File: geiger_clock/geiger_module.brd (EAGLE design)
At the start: 25 x 128.5 mm, 39 parts, among them IC2 7805TV, IC3 74125N, Q1 FJN3303F, Q2 2N3904, Q3 2N3904, U1 TLC555CP, U2 ATTINY2313, X1 8MHz

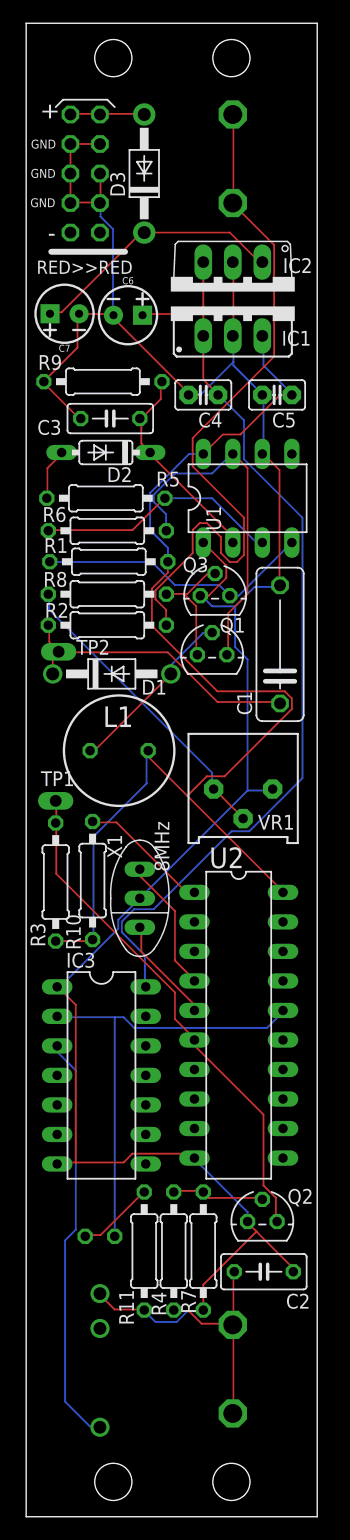
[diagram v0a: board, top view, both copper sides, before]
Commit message: updated the geiger module
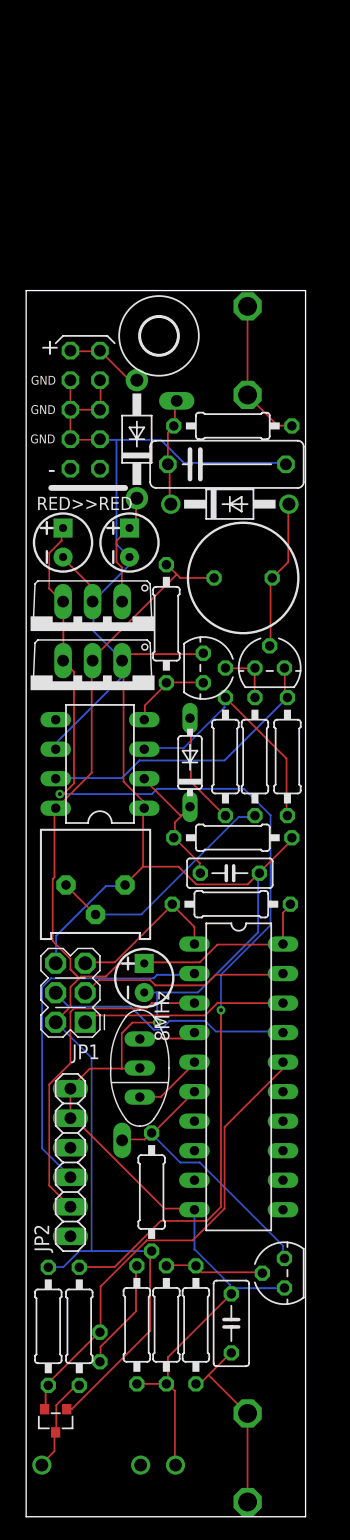
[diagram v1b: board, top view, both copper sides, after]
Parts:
- removed C5: 10uF, capacitor-wima:C2.5-2
- removed IC1: (no value), v-reg-3:78XXS
- added H1: MOUNT-HOLE3.2, holes:3,2
- added JP1: (no value), arduino_jw:CONN-2X03
- added JP2: (no value), pinhead:1X06
- added Q4: BSS138, bss138_10:SOT23
- added R12, R13: 10k, resistor:0207/10
- C4: device capacitor-wima:C2.5-2 -> SparkFun-Capacitors:CPOL-RADIAL-2.5MM-5MM
- IC3: value 74125N -> LM1117T(V)-3.3; device 74xx-us:DIL14 -> lm1117_10:TO220V
- moved C4 50.4 mm to (10.2, 46.4), turned to 90 degrees
- moved R9 40.8 mm to (17.8, 58.4), turned to 180 degrees
- moved C3 40.4 mm to (17.5, 55.4), turned to 0 degrees
- moved IC3 33.2 mm to (5.71, 71.1), turned to 180 degrees
- moved IC2 31.6 mm to (5.71, 76.2)
- moved TP1 29.8 mm to (8.26, 32.4), turned to 270 degrees
- moved R3 27.9 mm to (10.8, 27.9)
- moved D2 27.6 mm to (14.1, 64.9), turned to 90 degrees
- moved U1 26.2 mm to (6.35, 64.8), turned to 90 degrees
- moved R6 24.9 mm to (22.5, 65.4), turned to 90 degrees
- moved R5 24.5 mm to (17.1, 65.4), turned to 90 degrees
- moved TP2 23.9 mm to (13.0, 96.0)
- moved D3 22.9 mm to (9.53, 92.7)
- moved C7 20.5 mm to (8.89, 83.8), turned to 90 degrees
- moved C6 20.3 mm to (3.17, 83.8), turned to 90 degrees
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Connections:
- new net N$13: JP1.1, U2.18
- new net N$16: JP1.4, U2.17
- new net N$5: JP1.3, U2.19
- new net N$6: JP2.2, U2.3
- new net N$7: JP2.3, U2.2
- net 5V: now also IC3.3, R13.2; no longer C4.1, IC1.IN, IC3.14
- net GND: now also JP1.6, JP2.5, JP2.6; no longer C5.2, IC1.GND, IC3.7
- net N$2: now also JP1.5
- net PIN16: now also Q4.2, R12.1; no longer IC3.2
- net PIN165V: now also Q4.3, R13.1; no longer IC3.3
- net VCC: now also C4.1, IC3.2, JP1.2, Q4.1, R12.2; no longer C5.1, IC1.OUT
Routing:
- net N$15: track 61.1 -> 12.6 mm
- net N$7: track 0.00 -> 31.0 mm
- net N$6: track 0.00 -> 29.3 mm
- net PIN165V: track 35.5 -> 8.36 mm
- net N$16: track 0.00 -> 21.7 mm
- net GM_PULSE: track 44.1 -> 24.6 mm
- net VCC: track 100.6 -> 119.3 mm
- net N$5: track 0.00 -> 18.1 mm
- net N$13: track 0.00 -> 17.7 mm
- net N$3: track 23.9 -> 7.19 mm
- net HV: track 25.7 -> 9.36 mm
- net 5V: track 80.4 -> 94.1 mm, vias 0 -> 2
- net 12V: track 22.3 -> 9.86 mm
- net N$18: track 11.6 -> 4.95 mm
- net N$9: track 18.0 -> 11.8 mm
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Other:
- board size 25 x 128.5 mm -> 24 x 105.5 mm
